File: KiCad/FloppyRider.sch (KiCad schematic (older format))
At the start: 25 parts, among them J1 PC disk controller interface, J2 IBM Diskette Host power, J3 IBM 51TD Diskette unit, J4 Alternative power connector, SW1 Reset, U1 74LS08, U2 74LS02, U3 74LS06, U4 74LS74

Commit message: Changes for initial release
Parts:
- added R11, R8, R9: 1K, Resistor_SMD:R_0603_1608Metric, symbol Device:R
- R10, R5, R6, R7: value 4,7K -> 1K
- renumbered R9 to R12, R8 to R13
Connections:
- net VCC: now also R11.1, R8.1, R9.1
- net direction: now also R8.2
- net disk_chng_rdy: now also R1.2; no longer R4.2
- net drive_b: now also R10.2; no longer R7.2
- net head_1_select: now also R2.2
- net index: now also R11.2; no longer R1.2
- net motor_b: now also R9.2; no longer R6.2
- net read_data: now also R3.2; no longer R2.2
- net step: now also R7.2; no longer R10.2
- net track_0: now also R4.2; no longer R3.2
- net write_data: now also R6.2
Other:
- moved on the sheet: B1, R12, U1A, U1B, U1C, U1D, U2A, U2B, U2C, U2D, U3A, U3B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

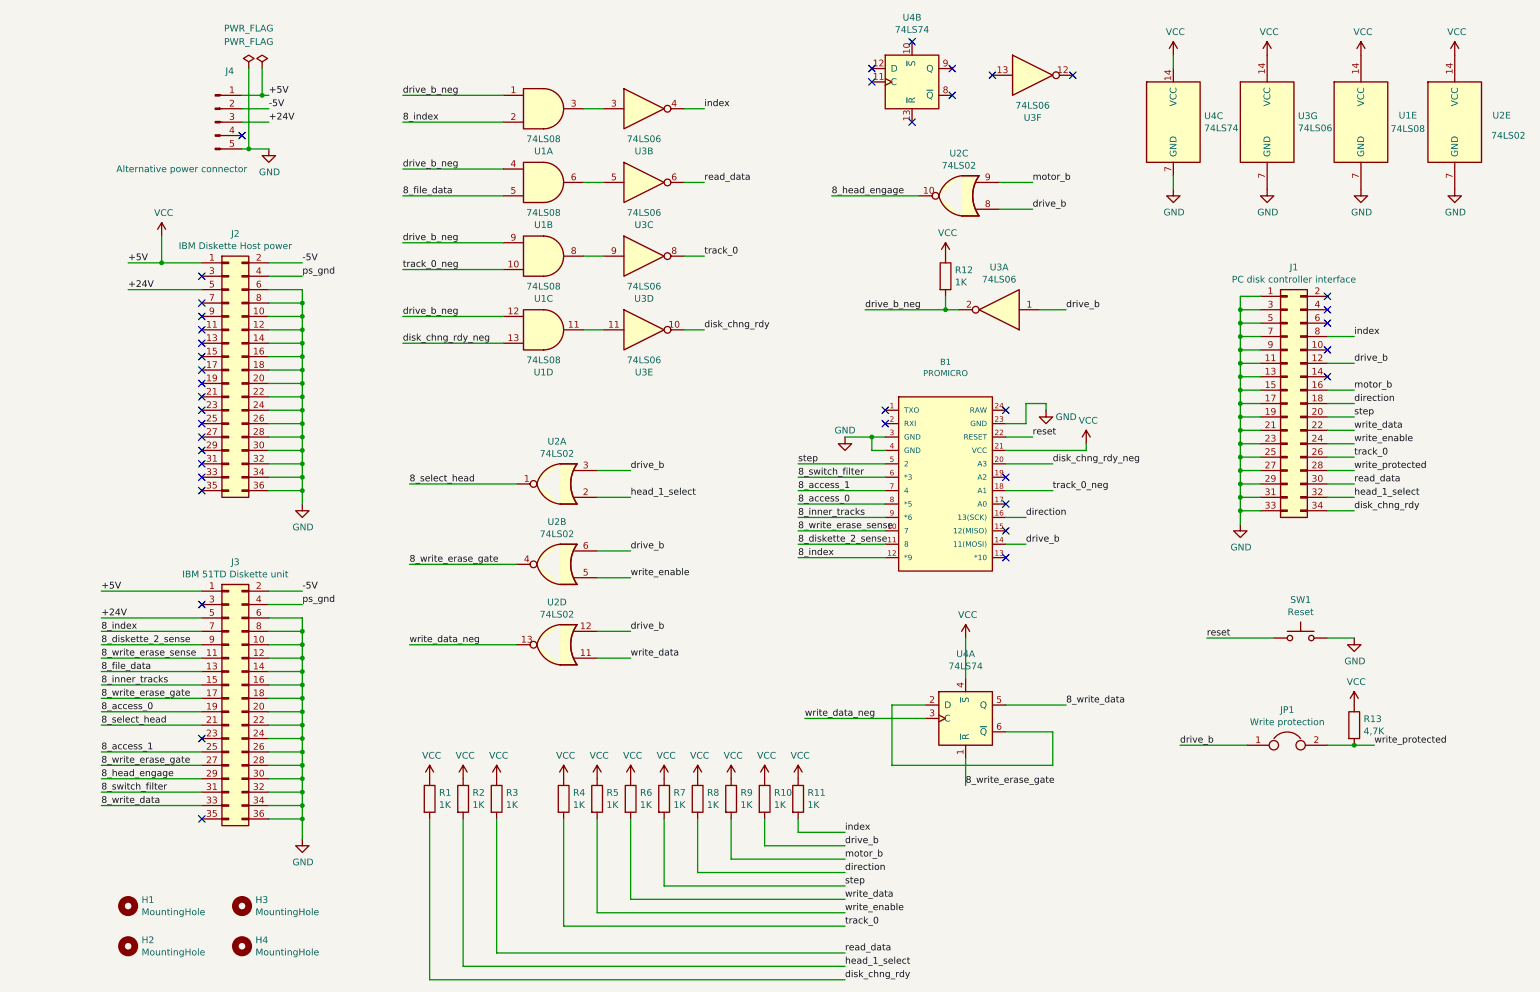
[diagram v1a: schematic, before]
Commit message: Added transistor to drive write/erase gate signals
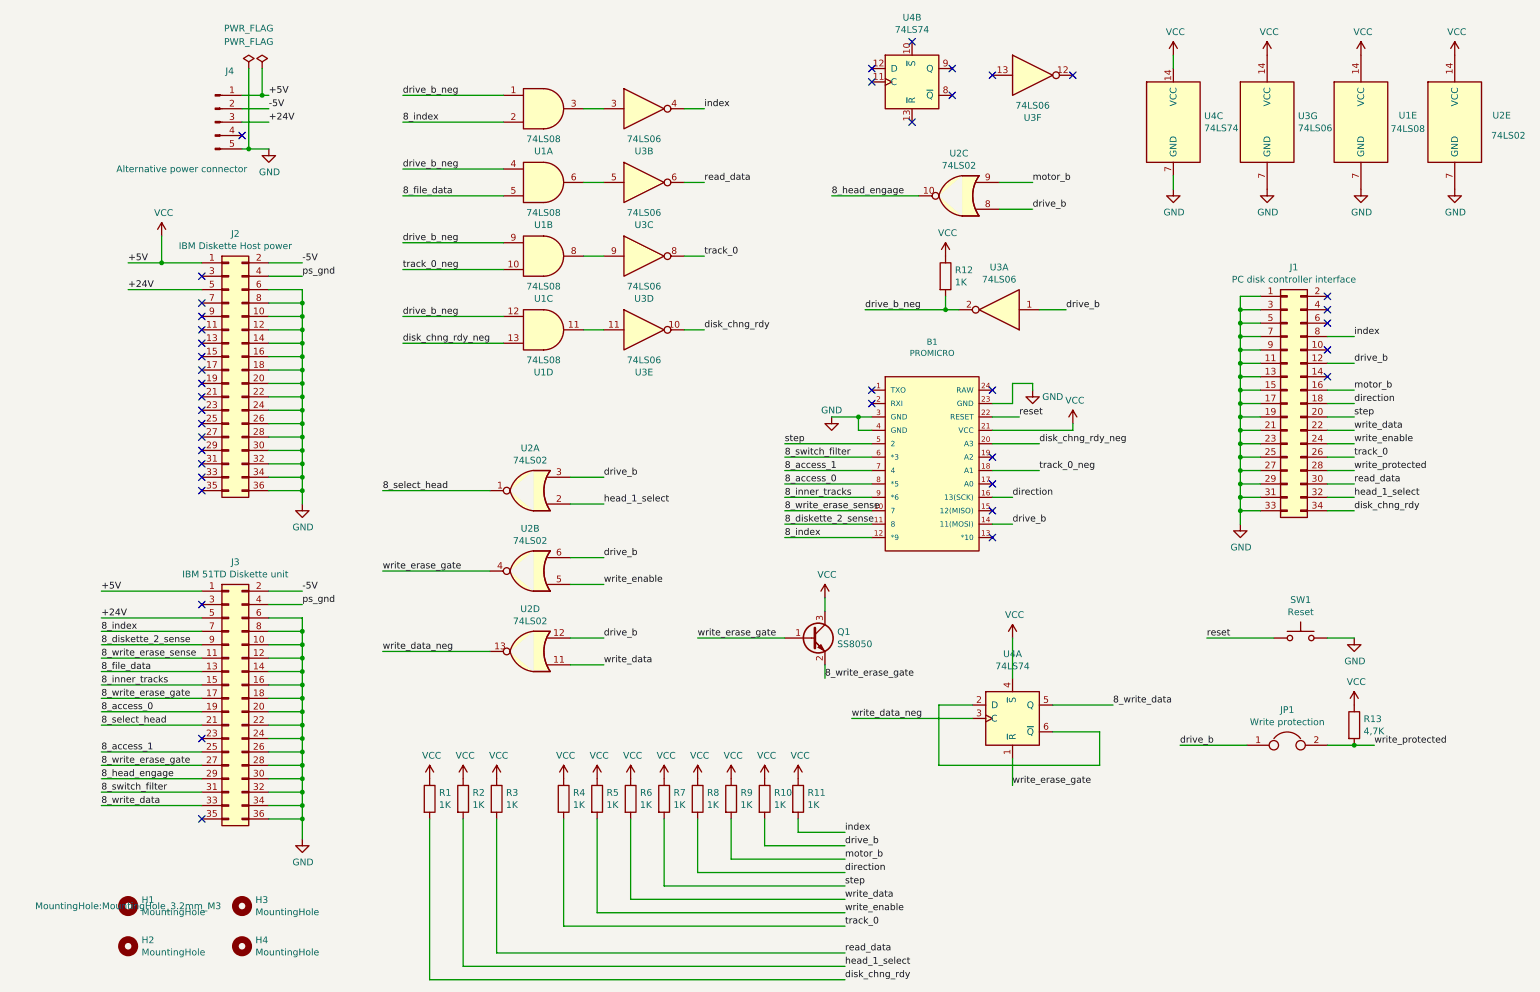
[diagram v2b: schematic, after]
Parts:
- added Q1: SS8050, Package_TO_SOT_SMD:SOT-23, symbol Transistor_BJT:2SC1945
- H1, H2, H3, H4: footprint MountingHole:MountingHole_2.2mm_M2 -> MountingHole:MountingHole_3.2mm_M3
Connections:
- net 8_write_erase_gate: now also Q1.2 (E); no longer U2.4, U4.1 (~R)
- net VCC: now also Q1.3 (C)
- new net write_erase_gate: Q1.1 (B), U2.4, U4.1 (~R)
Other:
- moved on the sheet: B1, U2A, U2B, U2D, U4A

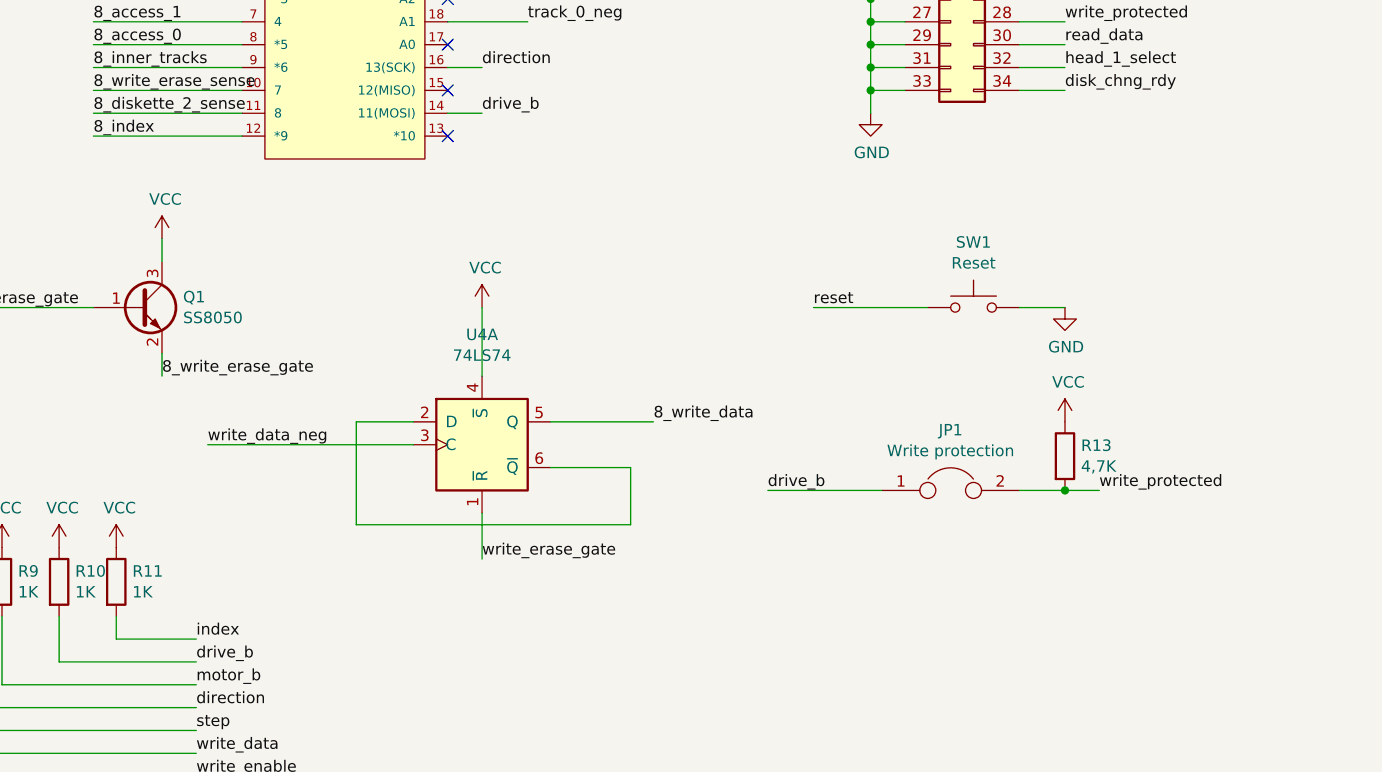
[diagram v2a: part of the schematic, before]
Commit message: Added hard write protection switch
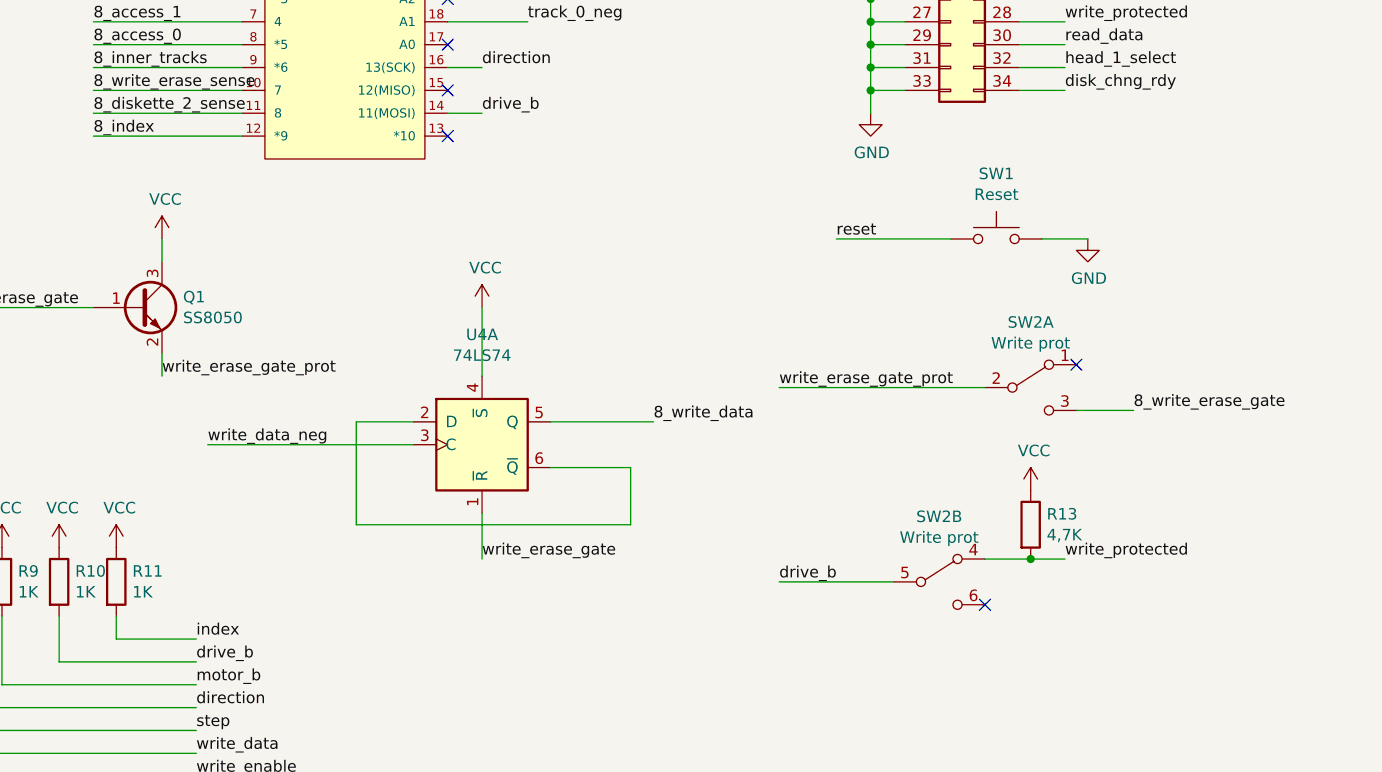
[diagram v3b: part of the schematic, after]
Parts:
- removed JP1: Write protection, Connector_PinHeader_2.54mm:PinHeader_1x02_P2.54mm_Vertical, symbol Device:Jumper
- added SW2: Write prot, dpdt_2:SW-TH_K3-2235S-K1, symbol Switch:SW_DPDT_x2
- R1, R10, R11, R12, R2, R3, R4, R5, R6, R7, R8, R9: LCSC (none) -> C21190
- R13: LCSC (none) -> C23162
- SW1: LCSC (none) -> C221880
- U1: LCSC (none) -> C6802
- U2: LCSC (none) -> C6794
- U3: LCSC (none) -> C113682
- U4: LCSC (none) -> C39990
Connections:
- net 8_write_erase_gate: now also SW2.3 (C); no longer Q1.2 (E)
- net drive_b: now also SW2.5 (B)
- net write_protected: now also SW2.4 (A)
- new net write_erase_gate_prot: Q1.2 (E), SW2.2 (B)
- no-connect marks 40 -> 42
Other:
- moved on the sheet: R13, SW1
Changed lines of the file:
@@
 F 2 "Package_SO:SO-14_3.9x8.65mm_P1.27mm" H 3900 1200 50  0001 C CNN
 F 3 "http://www.ti.com/lit/gpn/sn74LS33" H 3900 1200 50  0001 C CNN
+F 4 "C6802" H 3900 1200 50  0001 C CNN "LCSC"
 	1    3900 1200
 	1    0    0    -1
@@
 F 2 "Package_SO:SO-14_3.9x8.65mm_P1.27mm" H 3800 4050 50  0001 C CNN
 F 3 "http://www.ti.com/lit/gpn/sn74ls02" H 3800 4050 50  0001 C CNN
+F 4 "C6794" H 3800 4050 50  0001 C CNN "LCSC"
 	1    3800 4050
 	-1   0    0    1
@@
 Wire Wire Line
 	2700 5250 3500 5250
-Text Label 10100 5950 0    50   ~ 0
+Text Label 9950 6250 0    50   ~ 0
 write_protected
 Wire Wire Line
@@
 L Switch:SW_Push SW1
 U 1 1 629F7CD2
-P 9550 5150
-F 0 "SW1" H 9550 5435 50  0000 C CNN
-F 1 "Reset" H 9550 5344 50  0000 C CNN
-F 2 "Button_Switch_SMD:SW_Push_1P1T_NO_6x6mm_H9.5mm" H 9550 5350 50  0001 C CNN
-F 3 "~" H 9550 5350 50  0001 C CNN
-	1    9550 5150
+P 9650 4850
+F 0 "SW1" H 9650 5135 50  0000 C CNN
+F 1 "Reset" H 9650 5044 50  0000 C CNN
+F 2 "Button_Switch_SMD:SW_Push_1P1T_NO_6x6mm_H9.5mm" H 9650 5050 50  0001 C CNN
+F 3 "~" H 9650 5050 50  0001 C CNN
+F 4 "C221880" H 9650 4850 50  0001 C CNN "LCSC"
+	1    9650 4850
 	1    0    0    -1
 $EndComp
@@
 L power:GND #PWR022
 U 1 1 62A2D6E6
-P 9950 5150
-F 0 "#PWR022" H 9950 4900 50  0001 C CNN
-F 1 "GND" H 9955 4977 50  0000 C CNN
-F 2 "" H 9950 5150 50  0001 C CNN
-F 3 "" H 9950 5150 50  0001 C CNN
-	1    9950 5150
-	1    0    0    -1
-$EndComp
-Wire Wire Line
-	9750 5150 9950 5150
+P 10050 4850
+F 0 "#PWR022" H 10050 4600 50  0001 C CNN
+F 1 "GND" H 10055 4677 50  0000 C CNN
+F 2 "" H 10050 4850 50  0001 C CNN
+F 3 "" H 10050 4850 50  0001 C CNN
+	1    10050 4850
+	1    0    0    -1
+$EndComp
+Wire Wire Line
+	9850 4850 10050 4850
 Wire Wire Line
 	7400 3250 7550 3250
@@
 Wire Wire Line
 	7250 3500 7450 3500
-Text Label 8850 5150 0    50   ~ 0
+Text Label 8950 4850 0    50   ~ 0
 reset
 Wire Wire Line
-	8850 5150 9350 5150
+	8950 4850 9450 4850
 Text Label 4350 4750 0    50   ~ 0
 write_enable
@@
 F 2 "Package_SO:SO-14_3.9x8.65mm_P1.27mm" H 7300 2700 50  0001 C CNN
 F 3 "http://www.ti.com/lit/gpn/sn74LS04" H 7300 2700 50  0001 C CNN
+F 4 "C113682" H 7300 2700 50  0001 C CNN "LCSC"
 	1    7300 2700
 	-1   0    0    1
@@
 F 2 "Resistor_SMD:R_0603_1608Metric" V 6830 2450 50  0001 C CNN
 F 3 "~" H 6900 2450 50  0001 C CNN
+F 4 "C21190" H 6900 2450 50  0001 C CNN "LCSC"
 	1    6900 2450
 	1    0    0    -1
@@
 	1    0    0    -1
 $EndComp
-$Comp
-L Device:Jumper JP1
-U 1 1 62DF8DF2
-P 9450 5950
-F 0 "JP1" H 9450 6214 50  0000 C CNN
-F 1 "Write protection" H 9450 6123 50  0000 C CNN
-F 2 "Connector_PinHeader_2.54mm:PinHeader_1x02_P2.54mm_Vertical" H 9450 5950 50  0001 C CNN
-F 3 "~" H 9450 5950 50  0001 C CNN
-	1    9450 5950
-	1    0    0    -1
-$EndComp
-Wire Wire Line
-	8650 5950 9150 5950
-Text Label 8650 5950 0    50   ~ 0
+Wire Wire Line
+	8700 6350 9200 6350
+Text Label 8700 6350 0    50   ~ 0
 drive_b
 Wire Wire Line
@@
 F 2 "Package_SO:SO-14_3.9x8.65mm_P1.27mm" H 7400 5750 50  0001 C CNN
 F 3 "74xx/74hc_hct74.pdf" H 7400 5750 50  0001 C CNN
+F 4 "C39990" H 7400 5750 50  0001 C CNN "LCSC"
 	1    7400 5750
 	1    0    0    -1
@@
 L power:VCC #PWR023
 U 1 1 629E7594
-P 9950 5650
-F 0 "#PWR023" H 9950 5500 50  0001 C CNN
-F 1 "VCC" H 9965 5823 50  0000 C CNN
-F 2 "" H 9950 5650 50  0001 C CNN
-F 3 "" H 9950 5650 50  0001 C CNN
-	1    9950 5650
-	1    0    0    -1
-$EndComp
-Wire Wire Line
-	9750 5950 9950 5950
-Wire Wire Line
-	9950 5950 10100 5950
-Connection ~ 9950 5950
+P 9800 5950
+F 0 "#PWR023" H 9800 5800 50  0001 C CNN
+F 1 "VCC" H 9815 6123 50  0000 C CNN
+F 2 "" H 9800 5950 50  0001 C CNN
+F 3 "" H 9800 5950 50  0001 C CNN
+	1    9800 5950
+	1    0    0    -1
+$EndComp
+Wire Wire Line
+	9600 6250 9800 6250
+Wire Wire Line
+	9800 6250 9950 6250
+Connection ~ 9800 6250
 $Comp
 L Device:R R13
 U 1 1 629E6473
-P 9950 5800
-F 0 "R13" H 10020 5846 50  0000 L CNN
-F 1 "4,7K" H 10020 5755 50  0000 L CNN
-F 2 "Resistor_SMD:R_0603_1608Metric" V 9880 5800 50  0001 C CNN
-F 3 "~" H 9950 5800 50  0001 C CNN
-	1    9950 5800
+P 9800 6100
+F 0 "R13" H 9870 6146 50  0000 L CNN
+F 1 "4,7K" H 9870 6055 50  0000 L CNN
+F 2 "Resistor_SMD:R_0603_1608Metric" V 9730 6100 50  0001 C CNN
+F 3 "~" H 9800 6100 50  0001 C CNN
+F 4 "C23162" H 9800 6100 50  0001 C CNN "LCSC"
+	1    9800 6100
 	1    0    0    -1
 $EndComp
@@
 F 2 "Resistor_SMD:R_0603_1608Metric" V 5730 6350 50  0001 C CNN
 F 3 "~" H 5800 6350 50  0001 C CNN
+F 4 "C21190" H 5800 6350 50  0001 C CNN "LCSC"
 	1    5800 6350
 	1    0    0    -1
@@
 F 2 "Resistor_SMD:R_0603_1608Metric" V 5480 6350 50  0001 C CNN
 F 3 "~" H 5550 6350 50  0001 C CNN
+F 4 "C21190" H 5550 6350 50  0001 C CNN "LCSC"
 	1    5550 6350
 	1    0    0    -1
@@
 F 2 "Resistor_SMD:R_0603_1608Metric" V 5230 6350 50  0001 C CNN
 F 3 "~" H 5300 6350 50  0001 C CNN
+F 4 "C21190" H 5300 6350 50  0001 C CNN "LCSC"
 	1    5300 6350
 	1    0    0    -1
@@
 F 2 "Resistor_SMD:R_0603_1608Metric" V 4980 6350 50  0001 C CNN
 F 3 "~" H 5050 6350 50  0001 C CNN
+F 4 "C21190" H 5050 6350 50  0001 C CNN "LCSC"
 	1    5050 6350
 	1    0    0    -1
@@
 F 2 "Resistor_SMD:R_0603_1608Metric" V 4730 6350 50  0001 C CNN
 F 3 "~" H 4800 6350 50  0001 C CNN
+F 4 "C21190" H 4800 6350 50  0001 C CNN "LCSC"
 	1    4800 6350
 	1    0    0    -1
@@
 F 2 "Resistor_SMD:R_0603_1608Metric" V 4480 6350 50  0001 C CNN
 F 3 "~" H 4550 6350 50  0001 C CNN
+F 4 "C21190" H 4550 6350 50  0001 C CNN "LCSC"
 	1    4550 6350
 	1    0    0    -1
@@
 F 2 "Resistor_SMD:R_0603_1608Metric" V 4230 6350 50  0001 C CNN
 F 3 "~" H 4300 6350 50  0001 C CNN
+F 4 "C21190" H 4300 6350 50  0001 C CNN "LCSC"
 	1    4300 6350
 	1    0    0    -1
@@
 F 2 "Resistor_SMD:R_0603_1608Metric" V 3980 6350 50  0001 C CNN
 F 3 "~" H 4050 6350 50  0001 C CNN
+F 4 "C21190" H 4050 6350 50  0001 C CNN "LCSC"
 	1    4050 6350
 	1    0    0    -1
@@
 F 2 "Resistor_SMD:R_0603_1608Metric" V 3480 6350 50  0001 C CNN
 F 3 "~" H 3550 6350 50  0001 C CNN
+F 4 "C21190" H 3550 6350 50  0001 C CNN "LCSC"
 	1    3550 6350
 	1    0    0    -1
@@
 F 2 "Resistor_SMD:R_0603_1608Metric" V 3230 6350 50  0001 C CNN
 F 3 "~" H 3300 6350 50  0001 C CNN
+F 4 "C21190" H 3300 6350 50  0001 C CNN "LCSC"
 	1    3300 6350
 	1    0    0    -1
@@
 F 2 "Resistor_SMD:R_0603_1608Metric" V 2980 6350 50  0001 C CNN
 F 3 "~" H 3050 6350 50  0001 C CNN
+F 4 "C21190" H 3050 6350 50  0001 C CNN "LCSC"
 	1    3050 6350
 	1    0    0    -1
@@
 $EndComp
 Text Label 6000 5450 0    50   ~ 0
-8_write_erase_gate
+write_erase_gate_prot
 Text Label 5050 5150 0    50   ~ 0
 write_erase_gate
@@
 	6000 4850 6000 4950
 $Comp
+L Switch:SW_DPDT_x2 SW2
+U 2 1 62D549F3
+P 9400 6350
+F 0 "SW2" H 9400 6635 50  0000 C CNN
+F 1 "Write prot" H 9400 6544 50  0000 C CNN
+F 2 "dpdt_2:SW-TH_K3-2235S-K1" H 9400 6350 50  0001 C CNN
+F 3 "~" H 9400 6350 50  0001 C CNN
+	2    9400 6350
+	1    0    0    -1
+$EndComp
+$Comp
+L Switch:SW_DPDT_x2 SW2
+U 1 1 62D55E5C
+P 9800 5500
+F 0 "SW2" H 9800 5785 50  0000 C CNN
+F 1 "Write prot" H 9800 5694 50  0000 C CNN
+F 2 "dpdt_2:SW-TH_K3-2235S-K1" H 9800 5500 50  0001 C CNN
+F 3 "~" H 9800 5500 50  0001 C CNN
+F 4 "C223859" H 9800 5500 50  0001 C CNN "LCSC"
+	1    9800 5500
+	1    0    0    -1
+$EndComp
+Text Label 8700 5500 0    50   ~ 0
+write_erase_gate_prot
+Wire Wire Line
+	8700 5500 9600 5500
+Text Label 10250 5600 0    50   ~ 0
+8_write_erase_gate
+NoConn ~ 10000 5400
+NoConn ~ 9600 6450
+Wire Wire Line
+	10000 5600 10250 5600
+$Comp
 L Transistor_BJT:2SC1945 Q1
